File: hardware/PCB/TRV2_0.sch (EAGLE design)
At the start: 54 parts, among them IC1 TMP112, IC2 SHT21, IC4 CNY70, IC5 ATMEGA8-AU, Q1 FC-12M, U1 DRV8850_RGY_24

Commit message: changes as pr deniz requests
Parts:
- removed C3: 2.2uF, resistor:C-EUC0603
- removed R15: 1K, resistor:R-EU_R0603
- removed R4: 3K, resistor:R-EU_R0603
- IC2: value SHT21 -> IC2
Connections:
- removed net N$14: R15.2, R4.1, U1.LDOFB
- removed net N$15: C3.1, R4.2, U1.LDOOUT
- net GND: no longer C3.2, R15.1
- net MC: no longer IC4.COL, IC5.ANALOG_6, R14.1
- net MI: now also IC4.COL, IC5.ANALOG_6, R14.1
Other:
- note added: "IC1"
- note added: "IC2"
- moved on the sheet: C5
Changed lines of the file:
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@@
 </classes>
 <parts>
-<part name="IC2" library="SHT21" deviceset="SHT21" device=""/>
+<part name="IC2" library="SHT21" deviceset="SHT21" device="" value="IC2"/>
 <part name="GND1" library="supply1" deviceset="GND" device=""/>
 <part name="IC1" library="TMP112" deviceset="TMP112" device=""/>
@@
 <part name="R3" library="resistor" deviceset="R-EU_" device="R0603" value="24K"/>
 <part name="GND14" library="SparkFun-Aesthetics" deviceset="GND" device=""/>
-<part name="R4" library="resistor" deviceset="R-EU_" device="R0603" value="3K"/>
-<part name="R15" library="resistor" deviceset="R-EU_" device="R0603" value="1K"/>
-<part name="GND15" library="SparkFun-Aesthetics" deviceset="GND" device=""/>
-<part name="C3" library="resistor" deviceset="C-EU" device="C0603" value="2.2uF"/>
 <part name="R16" library="resistor" deviceset="R-EU_" device="R0603" value="4.3K"/>
 <part name="GND18" library="SparkFun-Aesthetics" deviceset="GND" device=""/>
@@
 <sheet>
 <plain>
+<text x="26.67" y="252.476" size="1.778" layer="95">IC2</text>
+<text x="26.162" y="225.044" size="1.778" layer="95">IC1</text>
 </plain>
 <instances>
@@
 <attribute name="VALUE" x="319.278" y="176.53" size="1.778" layer="96" rot="R270"/>
 </instance>
-<instance part="GND14" gate="1" x="314.96" y="182.88" rot="R270"/>
-<instance part="R4" gate="G$1" x="302.26" y="177.8" smashed="yes">
-<attribute name="NAME" x="303.53" y="179.2986" size="1.778" layer="95"/>
-<attribute name="VALUE" x="298.45" y="179.578" size="1.778" layer="96"/>
-</instance>
-<instance part="R15" gate="G$1" x="289.56" y="177.8" smashed="yes">
-<attribute name="NAME" x="290.83" y="179.2986" size="1.778" layer="95"/>
-<attribute name="VALUE" x="285.75" y="179.578" size="1.778" layer="96"/>
-</instance>
-<instance part="GND15" gate="1" x="276.86" y="177.8" rot="R270"/>
-<instance part="C3" gate="G$1" x="297.18" y="190.5" rot="R270"/>
+<instance part="GND14" gate="1" x="320.04" y="182.88" rot="R90"/>
 <instance part="R16" gate="G$1" x="287.02" y="160.02" smashed="yes">
 <attribute name="NAME" x="288.29" y="161.5186" size="1.778" layer="95"/>
@@
 </instance>
 <instance part="GND18" gate="1" x="276.86" y="160.02" rot="R270"/>
-<instance part="C5" gate="G$1" x="266.7" y="132.08"/>
+<instance part="C5" gate="G$1" x="281.94" y="170.18" rot="R90"/>
 <instance part="C12" gate="G$1" x="261.62" y="152.4" rot="R90"/>
 <instance part="C13" gate="G$1" x="261.62" y="165.1" rot="R90"/>
@@
 <wire x1="281.94" y1="144.78" x2="266.7" y2="144.78" width="0.1524" layer="91"/>
 <junction x="281.94" y="144.78"/>
-<pinref part="C5" gate="G$1" pin="1"/>
-<wire x1="266.7" y1="144.78" x2="266.7" y2="134.62" width="0.1524" layer="91"/>
 <pinref part="C12" gate="G$1" pin="2"/>
 <wire x1="266.7" y1="144.78" x2="266.7" y2="152.4" width="0.1524" layer="91"/>
-<junction x="266.7" y="144.78"/>
 <pinref part="C13" gate="G$1" pin="2"/>
 <wire x1="266.7" y1="152.4" x2="266.7" y2="165.1" width="0.1524" layer="91"/>
 <junction x="266.7" y="152.4"/>
 <label x="264.16" y="175.26" size="1.778" layer="95"/>
-<wire x1="266.7" y1="165.1" x2="266.7" y2="175.26" width="0.1524" layer="91"/>
+<wire x1="266.7" y1="165.1" x2="266.7" y2="170.18" width="0.1524" layer="91"/>
 <junction x="266.7" y="165.1"/>
+<pinref part="C5" gate="G$1" pin="1"/>
+<wire x1="266.7" y1="170.18" x2="266.7" y2="175.26" width="0.1524" layer="91"/>
+<wire x1="279.4" y1="170.18" x2="266.7" y2="170.18" width="0.1524" layer="91"/>
+<junction x="266.7" y="170.18"/>
 </segment>
 </net>
@@
 </segment>
 <segment>
-<pinref part="R15" gate="G$1" pin="1"/>
-<pinref part="GND15" gate="1" pin="GND"/>
-<wire x1="279.4" y1="177.8" x2="284.48" y2="177.8" width="0.1524" layer="91"/>
-<pinref part="C3" gate="G$1" pin="2"/>
-<wire x1="292.1" y1="190.5" x2="284.48" y2="190.5" width="0.1524" layer="91"/>
-<wire x1="284.48" y1="190.5" x2="284.48" y2="177.8" width="0.1524" layer="91"/>
-<junction x="284.48" y="177.8"/>
-</segment>
-<segment>
 <pinref part="R16" gate="G$1" pin="1"/>
 <pinref part="GND18" gate="1" pin="GND"/>
@@
 <net name="MC" class="0">
 <segment>
-<pinref part="IC4" gate="G$1" pin="COL"/>
-<pinref part="R14" gate="G$1" pin="1"/>
-<wire x1="127" y1="238.76" x2="129.54" y2="238.76" width="0.1524" layer="91"/>
-<wire x1="129.54" y1="238.76" x2="129.54" y2="241.3" width="0.1524" layer="91"/>
-<wire x1="129.54" y1="238.76" x2="137.16" y2="238.76" width="0.1524" layer="91"/>
-<junction x="129.54" y="238.76"/>
-<label x="137.16" y="238.76" size="1.778" layer="95"/>
-</segment>
-<segment>
 <pinref part="U1" gate="A" pin="VPROPI"/>
 <wire x1="304.8" y1="144.78" x2="304.8" y2="154.94" width="0.1524" layer="91"/>
-<wire x1="304.8" y1="154.94" x2="292.1" y2="154.94" width="0.1524" layer="91"/>
+<wire x1="304.8" y1="154.94" x2="297.18" y2="154.94" width="0.1524" layer="91"/>
 <pinref part="R16" gate="G$1" pin="2"/>
+<wire x1="297.18" y1="154.94" x2="292.1" y2="154.94" width="0.1524" layer="91"/>
 <wire x1="292.1" y1="154.94" x2="292.1" y2="160.02" width="0.1524" layer="91"/>
-<label x="297.18" y="157.48" size="1.778" layer="95"/>
-</segment>
-<segment>
-<pinref part="IC5" gate="1" pin="ANALOG_6"/>
-<wire x1="152.4" y1="86.36" x2="160.02" y2="86.36" width="0.1524" layer="91"/>
-<label x="154.94" y="86.36" size="1.778" layer="95"/>
+<label x="297.942" y="162.052" size="1.778" layer="95"/>
+<wire x1="297.18" y1="154.94" x2="297.18" y2="162.56" width="0.1524" layer="91"/>
+<junction x="297.18" y="154.94"/>
+</segment>
+<segment>
+<wire x1="152.4" y1="83.82" x2="160.02" y2="83.82" width="0.1524" layer="91"/>
+<label x="154.94" y="83.82" size="1.778" layer="95"/>
 </segment>
 </net>
@@
 <segment>
 <pinref part="U1" gate="A" pin="NSLEEP"/>
-<wire x1="299.72" y1="165.1" x2="307.34" y2="165.1" width="0.1524" layer="91"/>
-<wire x1="307.34" y1="165.1" x2="307.34" y2="144.78" width="0.1524" layer="91"/>
-<label x="289.56" y="165.1" size="1.778" layer="95"/>
+<wire x1="307.34" y1="172.72" x2="307.34" y2="144.78" width="0.1524" layer="91"/>
+<label x="297.18" y="172.72" size="1.778" layer="95"/>
 </segment>
 </net>
@@
 <wire x1="43.18" y1="147.32" x2="50.8" y2="147.32" width="0.1524" layer="91"/>
 <label x="50.8" y="147.32" size="1.778" layer="95"/>
+</segment>
+<segment>
+<pinref part="IC4" gate="G$1" pin="COL"/>
+<pinref part="R14" gate="G$1" pin="1"/>
+<wire x1="127" y1="238.76" x2="129.54" y2="238.76" width="0.1524" layer="91"/>
+<wire x1="129.54" y1="238.76" x2="129.54" y2="241.3" width="0.1524" layer="91"/>
+<wire x1="129.54" y1="238.76" x2="137.16" y2="238.76" width="0.1524" layer="91"/>
+<junction x="129.54" y="238.76"/>
+<label x="137.16" y="238.76" size="1.778" layer="95"/>
+</segment>
+<segment>
+<pinref part="IC5" gate="1" pin="ANALOG_6"/>
+<wire x1="152.4" y1="86.36" x2="160.02" y2="86.36" width="0.1524" layer="91"/>
+<label x="154.94" y="86.36" size="1.778" layer="95"/>
 </segment>
 </net>
@@
 </segment>
 </net>
-<net name="N$14" class="0">
-<segment>
-<pinref part="R4" gate="G$1" pin="1"/>
-<pinref part="R15" gate="G$1" pin="2"/>
-<wire x1="297.18" y1="177.8" x2="294.64" y2="177.8" width="0.1524" layer="91"/>
-<wire x1="294.64" y1="177.8" x2="294.64" y2="170.18" width="0.1524" layer="91"/>
-<wire x1="294.64" y1="170.18" x2="312.42" y2="170.18" width="0.1524" layer="91"/>
-<junction x="294.64" y="177.8"/>
-<pinref part="U1" gate="A" pin="LDOFB"/>
-<wire x1="312.42" y1="170.18" x2="312.42" y2="144.78" width="0.1524" layer="91"/>
-</segment>
-</net>
-<net name="N$15" class="0">
-<segment>
-<pinref part="R4" gate="G$1" pin="2"/>
-<wire x1="307.34" y1="177.8" x2="307.34" y2="187.96" width="0.1524" layer="91"/>
-<wire x1="307.34" y1="187.96" x2="327.66" y2="187.96" width="0.1524" layer="91"/>
-<wire x1="327.66" y1="187.96" x2="327.66" y2="55.88" width="0.1524" layer="91"/>
-<wire x1="327.66" y1="55.88" x2="307.34" y2="55.88" width="0.1524" layer="91"/>
-<pinref part="U1" gate="A" pin="LDOOUT"/>
-<wire x1="307.34" y1="55.88" x2="307.34" y2="73.66" width="0.1524" layer="91"/>
-<wire x1="307.34" y1="73.66" x2="304.8" y2="73.66" width="0.1524" layer="91"/>
-<pinref part="C3" gate="G$1" pin="1"/>
-<wire x1="299.72" y1="190.5" x2="299.72" y2="187.96" width="0.1524" layer="91"/>
-<wire x1="299.72" y1="187.96" x2="307.34" y2="187.96" width="0.1524" layer="91"/>
-<junction x="307.34" y="187.96"/>
-</segment>
-</net>
 <net name="N$20" class="0">
 <segment>
 <pinref part="U1" gate="A" pin="VCP"/>
-<wire x1="314.96" y1="144.78" x2="314.96" y2="124.46" width="0.1524" layer="91"/>
-<wire x1="314.96" y1="124.46" x2="266.7" y2="124.46" width="0.1524" layer="91"/>
+<wire x1="314.96" y1="144.78" x2="314.96" y2="182.88" width="0.1524" layer="91"/>
+<wire x1="314.96" y1="182.88" x2="294.64" y2="182.88" width="0.1524" layer="91"/>
+<wire x1="294.64" y1="182.88" x2="294.64" y2="170.18" width="0.1524" layer="91"/>
 <pinref part="C5" gate="G$1" pin="2"/>
-<wire x1="266.7" y1="124.46" x2="266.7" y2="127" width="0.1524" layer="91"/>
-</segment>
-</net>
+<wire x1="294.64" y1="170.18" x2="287.02" y2="170.18" width="0.1524" layer="91"/>
+</segment>
+</net>

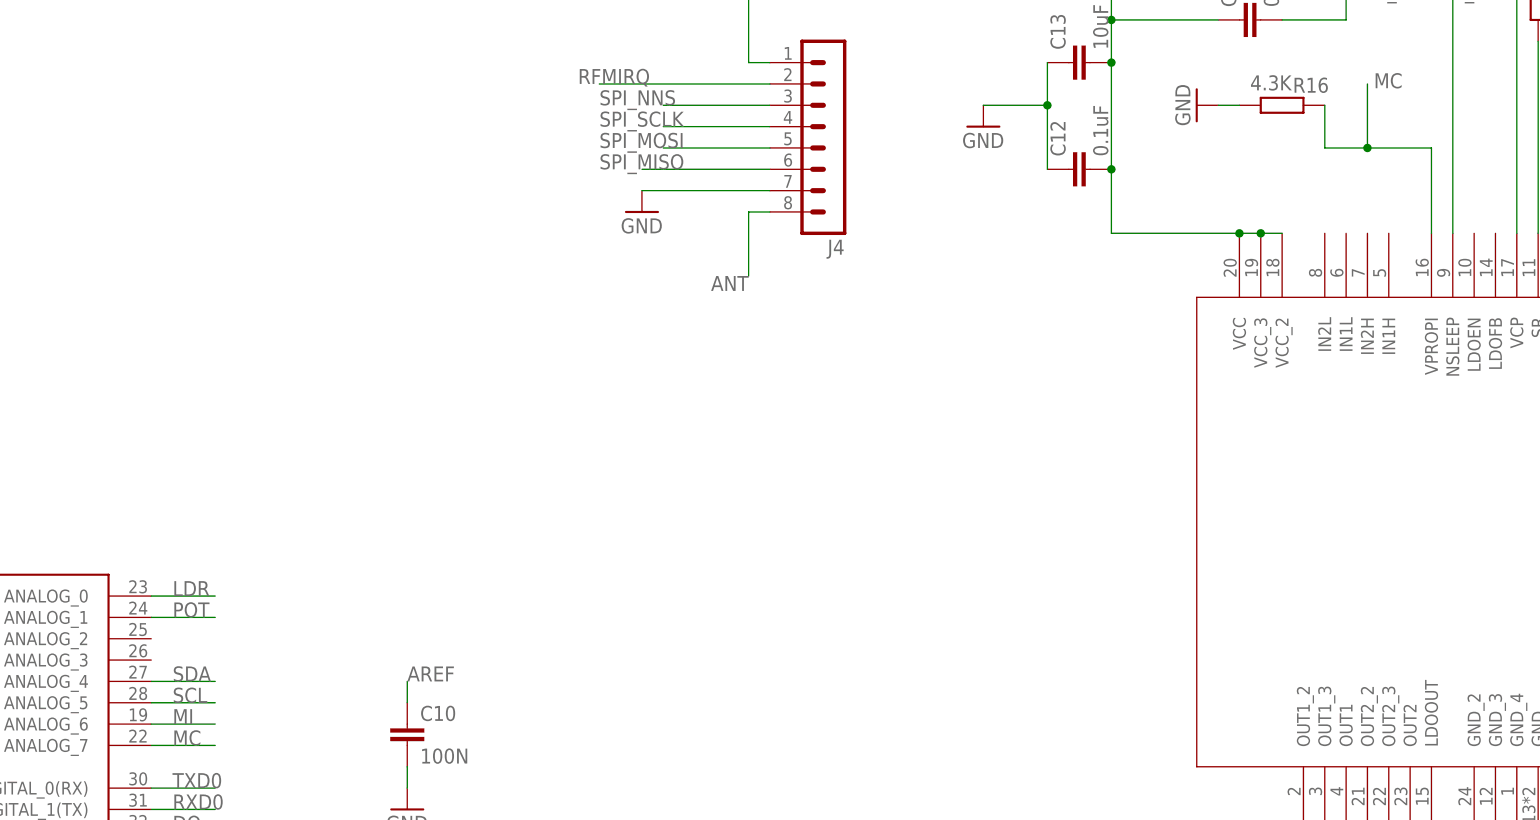
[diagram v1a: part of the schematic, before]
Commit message: Motor driver conncedted
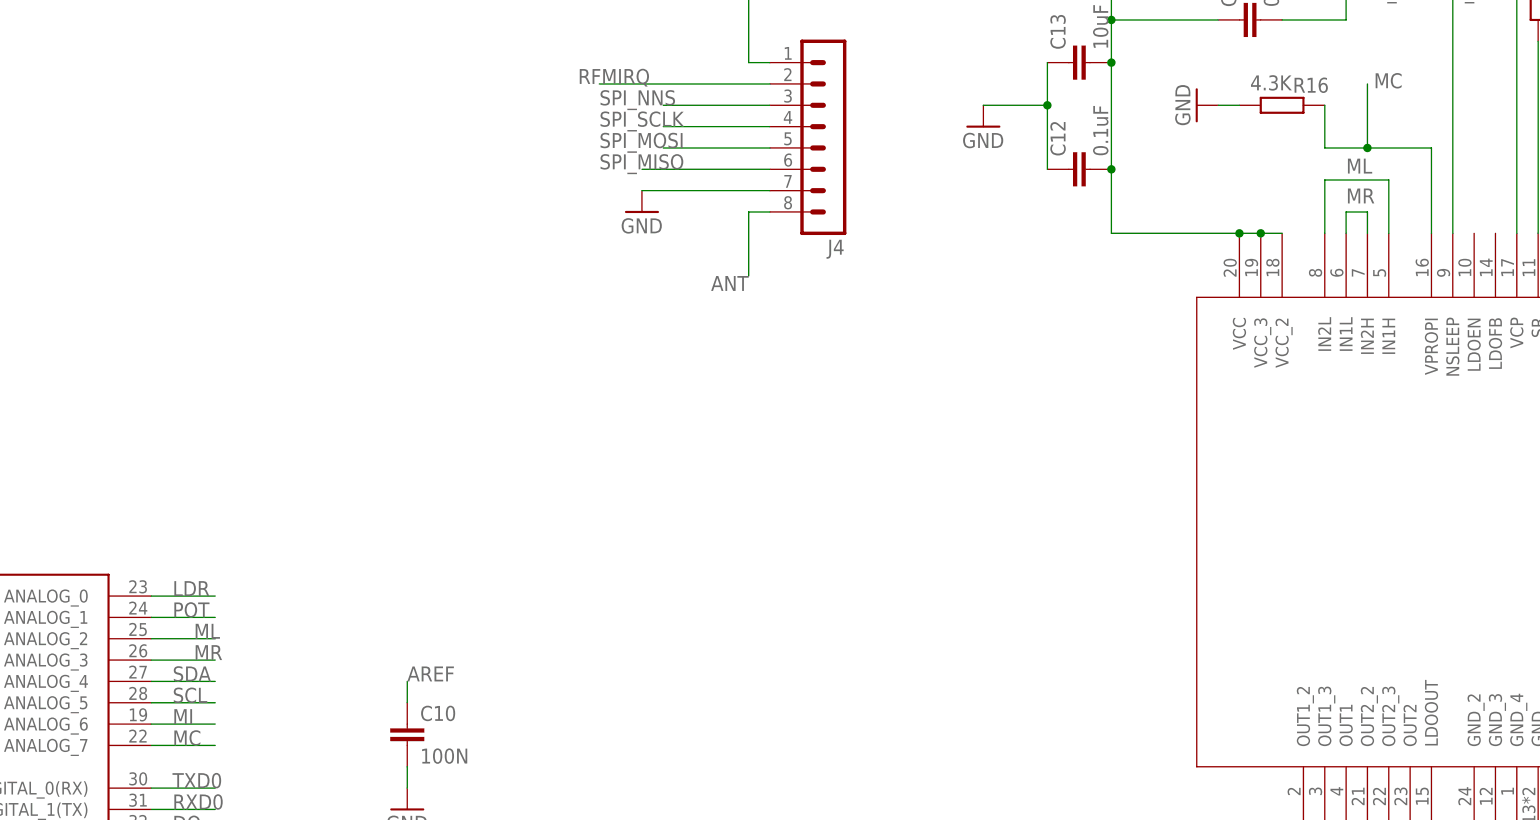
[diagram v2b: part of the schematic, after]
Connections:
- new net ML: IC5.ANALOG_2, U1.IN1H, U1.IN2L
- new net MR: IC5.ANALOG_3, U1.IN1L, U1.IN2H
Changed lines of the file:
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@@
+</segment>
+</net>
+<net name="ML" class="0">
+<segment>
+<pinref part="U1" gate="A" pin="IN1H"/>
+<wire x1="299.72" y1="144.78" x2="299.72" y2="151.13" width="0.1524" layer="91"/>
+<pinref part="U1" gate="A" pin="IN2L"/>
+<wire x1="299.72" y1="151.13" x2="292.1" y2="151.13" width="0.1524" layer="91"/>
+<wire x1="292.1" y1="151.13" x2="292.1" y2="144.78" width="0.1524" layer="91"/>
+<label x="294.64" y="151.892" size="1.778" layer="95"/>
+</segment>
+<segment>
+<pinref part="IC5" gate="1" pin="ANALOG_2"/>
+<wire x1="152.4" y1="96.52" x2="160.02" y2="96.52" width="0.1524" layer="91"/>
+<label x="157.48" y="96.52" size="1.778" layer="95"/>
+</segment>
+</net>
+<net name="MR" class="0">
+<segment>
+<pinref part="U1" gate="A" pin="IN1L"/>
+<wire x1="294.64" y1="144.78" x2="294.64" y2="147.32" width="0.1524" layer="91"/>
+<pinref part="U1" gate="A" pin="IN2H"/>
+<wire x1="294.64" y1="147.32" x2="297.18" y2="147.32" width="0.1524" layer="91"/>
+<wire x1="297.18" y1="147.32" x2="297.18" y2="144.78" width="0.1524" layer="91"/>
+<label x="294.64" y="148.336" size="1.778" layer="95"/>
+</segment>
+<segment>
+<pinref part="IC5" gate="1" pin="ANALOG_3"/>
+<wire x1="152.4" y1="93.98" x2="160.02" y2="93.98" width="0.1524" layer="91"/>
+<label x="157.48" y="93.98" size="1.778" layer="95"/>
 </segment>
 </net>

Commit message: Before routing tracks
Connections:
- net MC: now also IC5.ANALOG_7
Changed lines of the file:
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@@
 <wire x1="152.4" y1="83.82" x2="160.02" y2="83.82" width="0.1524" layer="91"/>
 <label x="154.94" y="83.82" size="1.778" layer="95"/>
+<pinref part="IC5" gate="1" pin="ANALOG_7"/>
 </segment>
 </net>
